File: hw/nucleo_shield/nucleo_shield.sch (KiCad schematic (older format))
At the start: 11 parts, among them CN101 Nucleo-F411RE-CN10, CN71 Nucleo-F411RE-CN7, P4 POWER_CON, P6 ETH_CONN, P7 SD_CONN, P8 LCD_CONN, P9 CONN_SCT

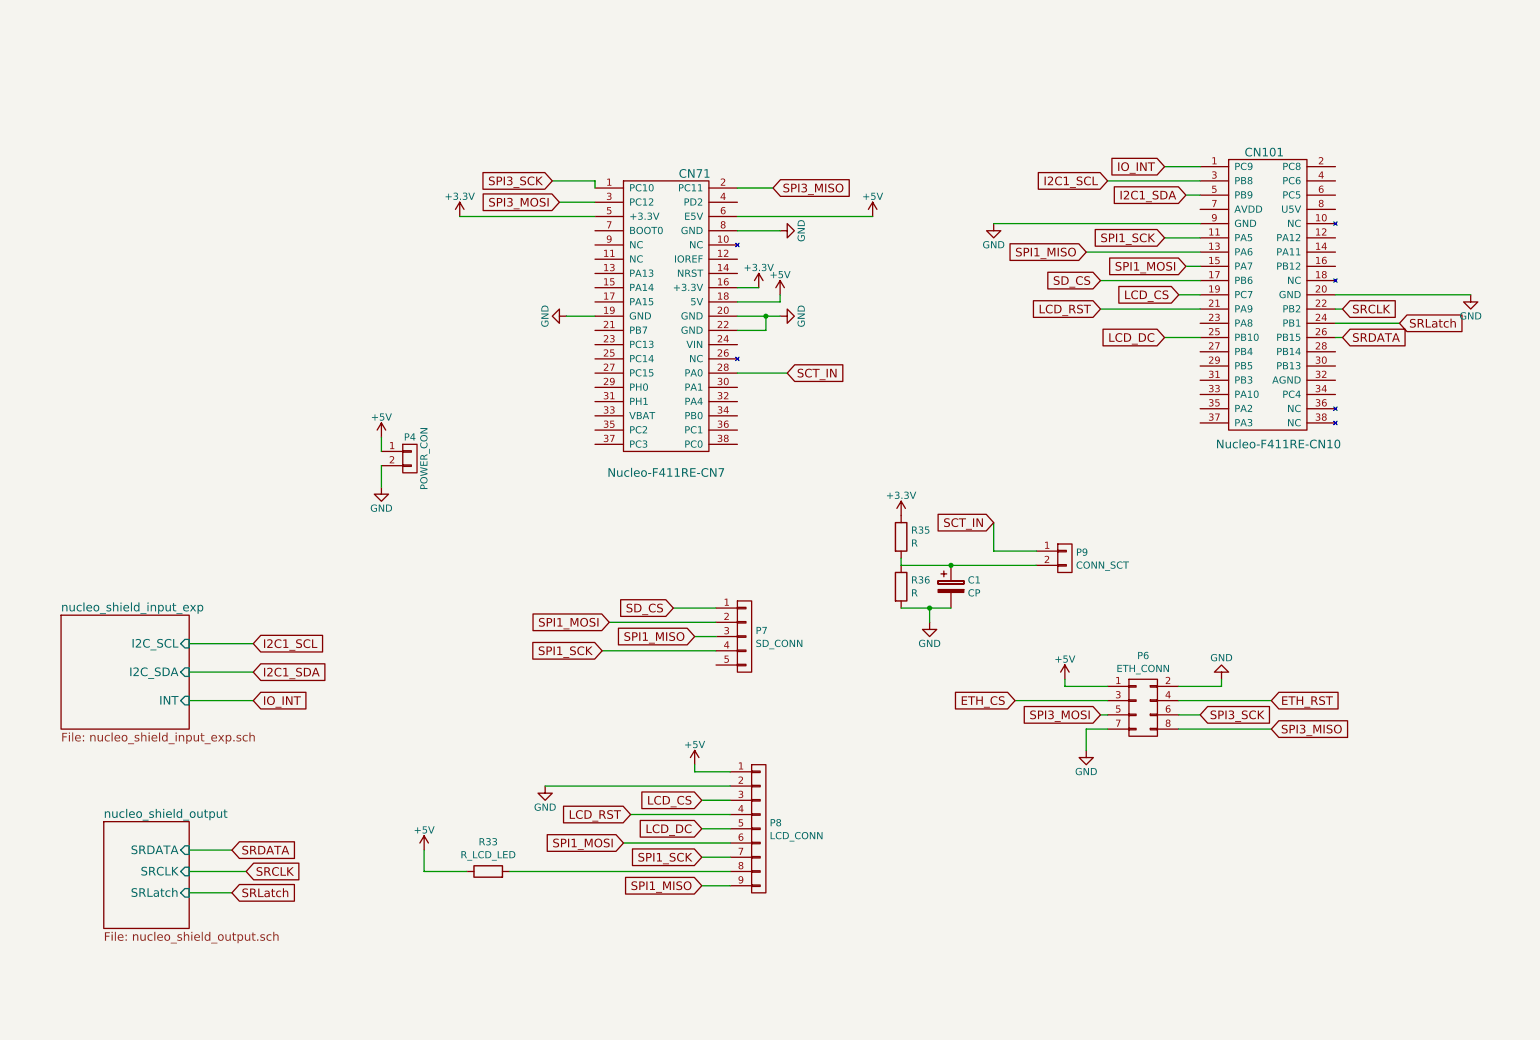
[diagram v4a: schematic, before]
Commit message: Nucleo: add RS485 headers, add CMS pulldown  resistors
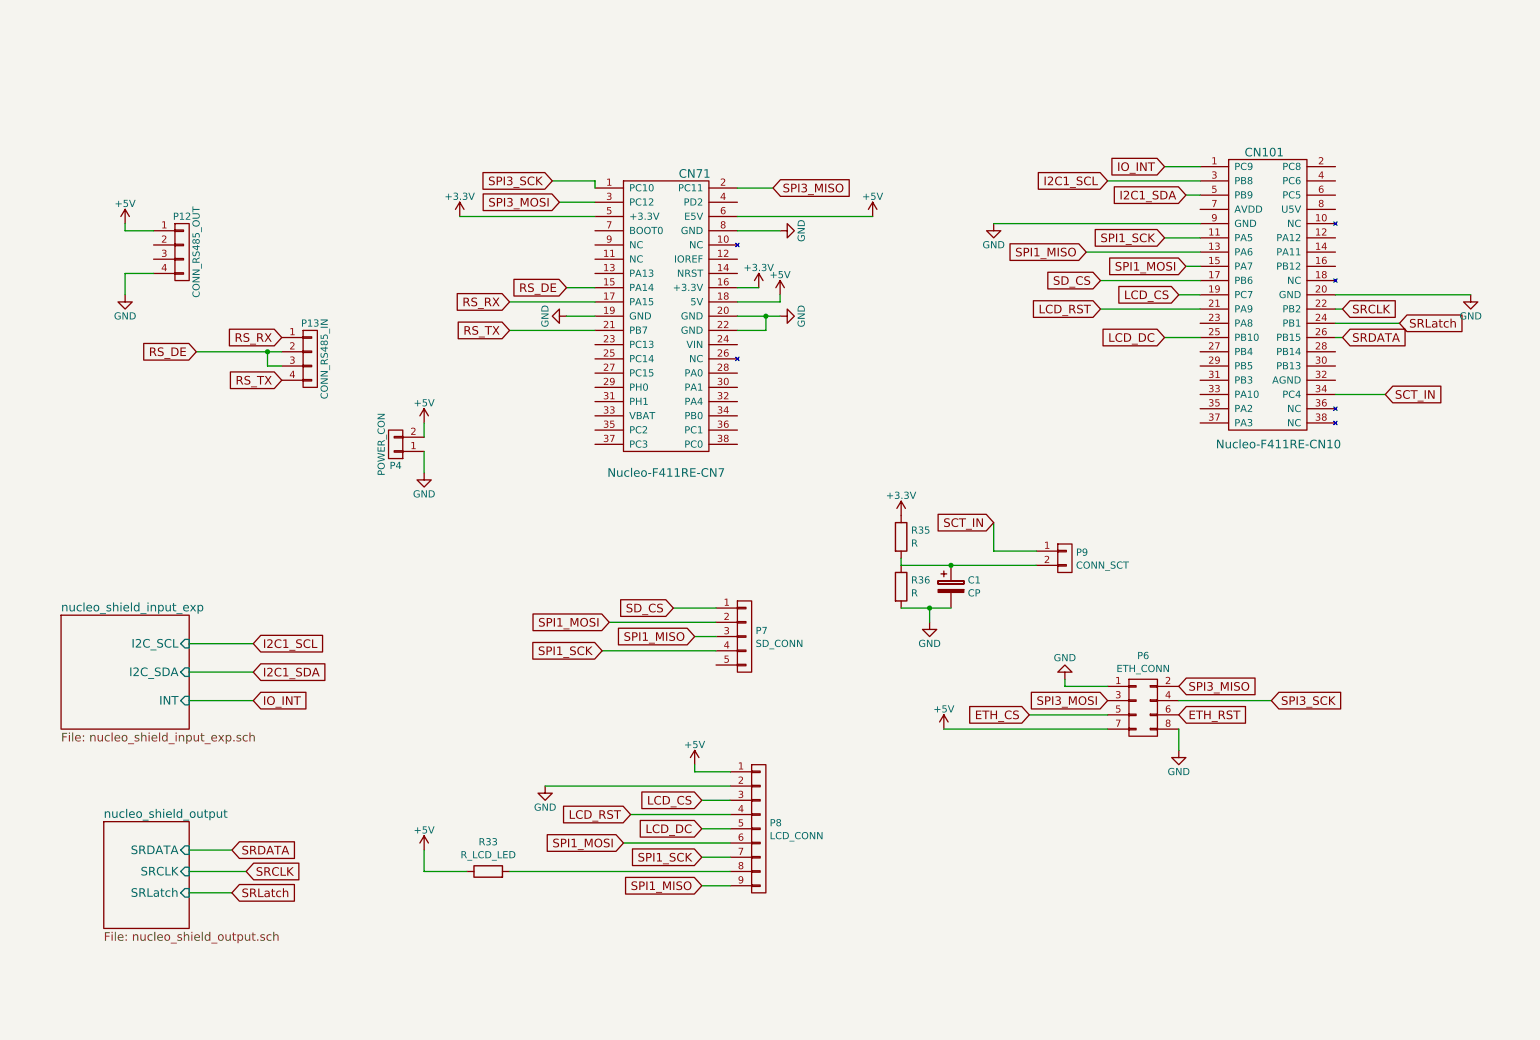
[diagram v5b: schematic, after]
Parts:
- added P12: CONN_RS485_OUT, Pin_Headers:Pin_Header_Straight_1x04, symbol CONN_01X04
- added P13: CONN_RS485_IN, Pin_Headers:Pin_Header_Straight_1x04, symbol CONN_01X04
- R33, R35, R36: footprint Resistors_ThroughHole:Resistor_Horizontal_RM10mm -> Resistors_SMD:R_0805_HandSoldering
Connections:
- net +5V: now also P4.2 (P2), P6.7 (P7), P12.1 (P1); no longer P4.1 (P1), P6.1 (P1)
- net ETH_CS: now also P6.5 (P5); no longer P6.3 (P3)
- net ETH_RST: now also P6.6 (P6); no longer P6.4 (P4)
- net GND: now also P4.1 (P1), P6.1 (P1), P6.8 (P8), P12.4 (P4); no longer P4.2 (P2), P6.2 (P2), P6.7 (P7)
- net SCT_IN: now also CN101.34 (PC4); no longer CN71.28 (PA0)
- net SPI3_MISO: now also P6.2 (P2); no longer P6.8 (P8)
- net SPI3_MOSI: now also P6.3 (P3); no longer P6.5 (P5)
- net SPI3_SCK: now also P6.4 (P4); no longer P6.6 (P6)
- net RS_DE: now reaches CN71.15 (PA14)
- net RS_DE: now also P13.2 (P2), P13.3 (P3)
- net RS_RX: now reaches CN71.17 (PA15)
- net RS_RX: now also P13.1 (P1)
- net RS_TX: now reaches CN71.21 (PB7)
- net RS_TX: now also P13.4 (P4)
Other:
- moved on the sheet: P4
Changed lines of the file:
@@
 LIBS:memory
 LIBS:xilinx
+LIBS:special
 LIBS:microcontrollers
 LIBS:dsp
@@
 L CONN_01X02 P4
 U 1 1 56AB61A1
-P 3400 3700
-F 0 "P4" H 3400 3850 50  0000 C CNN
-F 1 "POWER_CON" V 3500 3700 50  0000 C CNN
-F 2 "w_conn_screw:mors_2p" H 3400 3700 60  0001 C CNN
-F 3 "" H 3400 3700 60  0000 C CNN
-	1    3400 3700
-	1    0    0    -1
+P 3300 3600
+F 0 "P4" H 3300 3750 50  0000 C CNN
+F 1 "POWER_CON" V 3400 3600 50  0000 C CNN
+F 2 "w_conn_screw:mors_2p" H 3300 3600 60  0001 C CNN
+F 3 "" H 3300 3600 60  0000 C CNN
+	1    3300 3600
+	-1   0    0    1
 $EndComp
 $Comp
 L +5V #PWR09
 U 1 1 56AB6530
-P 3200 3550
-F 0 "#PWR09" H 3200 3400 50  0001 C CNN
-F 1 "+5V" H 3200 3690 50  0000 C CNN
-F 2 "" H 3200 3550 60  0000 C CNN
-F 3 "" H 3200 3550 60  0000 C CNN
-	1    3200 3550
+P 3500 3450
+F 0 "#PWR09" H 3500 3300 50  0001 C CNN
+F 1 "+5V" H 3500 3590 50  0000 C CNN
+F 2 "" H 3500 3450 60  0000 C CNN
+F 3 "" H 3500 3450 60  0000 C CNN
+	1    3500 3450
 	1    0    0    -1
 $EndComp
@@
 L GND #PWR010
 U 1 1 56AB6589
-P 3200 3900
-F 0 "#PWR010" H 3200 3650 50  0001 C CNN
-F 1 "GND" H 3200 3750 50  0000 C CNN
-F 2 "" H 3200 3900 60  0000 C CNN
-F 3 "" H 3200 3900 60  0000 C CNN
-	1    3200 3900
+P 3500 3800
+F 0 "#PWR010" H 3500 3550 50  0001 C CNN
+F 1 "GND" H 3500 3650 50  0000 C CNN
+F 2 "" H 3500 3800 60  0000 C CNN
+F 3 "" H 3500 3800 60  0000 C CNN
+	1    3500 3800
 	1    0    0    -1
 $EndComp
@@
 	9900 2850 9950 2850
 Wire Wire Line
-	3200 3650 3200 3550
-Wire Wire Line
-	3200 3750 3200 3900
+	3500 3550 3500 3450
+Wire Wire Line
+	3500 3650 3500 3800
 Wire Wire Line
 	3750 2000 4700 2000
@@
 L +5V #PWR012
 U 1 1 572A65CF
+P 7150 5600
+F 0 "#PWR012" H 7150 5450 50  0001 C CNN
+F 1 "+5V" H 7150 5740 50  0000 C CNN
+F 2 "" H 7150 5600 60  0000 C CNN
+F 3 "" H 7150 5600 60  0000 C CNN
+	1    7150 5600
+	1    0    0    -1
+$EndComp
+$Comp
+L GND #PWR013
+U 1 1 572A660A
 P 8000 5250
-F 0 "#PWR012" H 8000 5100 50  0001 C CNN
-F 1 "+5V" H 8000 5390 50  0000 C CNN
+F 0 "#PWR013" H 8000 5000 50  0001 C CNN
+F 1 "GND" H 8000 5100 50  0000 C CNN
 F 2 "" H 8000 5250 60  0000 C CNN
 F 3 "" H 8000 5250 60  0000 C CNN
 	1    8000 5250
-	1    0    0    -1
-$EndComp
-$Comp
-L GND #PWR013
-U 1 1 572A660A
-P 9100 5250
-F 0 "#PWR013" H 9100 5000 50  0001 C CNN
-F 1 "GND" H 9100 5100 50  0000 C CNN
-F 2 "" H 9100 5250 60  0000 C CNN
-F 3 "" H 9100 5250 60  0000 C CNN
-	1    9100 5250
-	-1   0    0    1
-$EndComp
-Wire Wire Line
-	8800 5300 9100 5300
-Wire Wire Line
-	9100 5300 9100 5250
-Wire Wire Line
-	8000 5250 8000 5300
-Wire Wire Line
-	8000 5300 8300 5300
-Text GLabel 9450 5400 2    60   Input ~ 0
+	1    0    0    1
+$EndComp
+Wire Wire Line
+	8300 5300 8000 5300
+Wire Wire Line
+	8000 5300 8000 5250
+Text GLabel 8800 5500 2    60   Input ~ 0
 ETH_RST
-Text GLabel 7650 5400 0    60   Input ~ 0
+Text GLabel 7750 5500 0    60   Input ~ 0
 ETH_CS
 $Comp
 L GND #PWR014
 U 1 1 572A6AC8
-P 8150 5750
-F 0 "#PWR014" H 8150 5500 50  0001 C CNN
-F 1 "GND" H 8150 5600 50  0000 C CNN
-F 2 "" H 8150 5750 60  0000 C CNN
-F 3 "" H 8150 5750 60  0000 C CNN
-	1    8150 5750
-	1    0    0    -1
-$EndComp
-Wire Wire Line
-	7650 5400 8300 5400
-Wire Wire Line
-	8250 5500 8300 5500
-Wire Wire Line
-	8300 5600 8150 5600
-Wire Wire Line
-	8150 5600 8150 5750
+P 8800 5750
+F 0 "#PWR014" H 8800 5500 50  0001 C CNN
+F 1 "GND" H 8800 5600 50  0000 C CNN
+F 2 "" H 8800 5750 60  0000 C CNN
+F 3 "" H 8800 5750 60  0000 C CNN
+	1    8800 5750
+	1    0    0    -1
+$EndComp
+Wire Wire Line
+	7750 5500 8300 5500
+Wire Wire Line
+	8800 5600 8800 5750
 Wire Wire Line
 	8800 5400 9450 5400
-Wire Wire Line
-	8950 5500 8800 5500
-Wire Wire Line
-	8800 5600 9450 5600
-Text GLabel 8950 5500 2    60   Input ~ 0
+Text GLabel 9450 5400 2    60   Input ~ 0
 SPI3_SCK
-Text GLabel 8250 5500 0    60   Input ~ 0
+Text GLabel 8300 5400 0    60   Input ~ 0
 SPI3_MOSI
-Text GLabel 9450 5600 2    60   Input ~ 0
+Text GLabel 8800 5300 2    60   Input ~ 0
 SPI3_MISO
 Text GLabel 8700 2150 0    60   Input ~ 0
@@
 F 0 "R33" V 4157 6600 50  0000 C CNN
 F 1 "R_LCD_LED" V 4066 6600 50  0000 C CNN
-F 2 "Resistors_ThroughHole:Resistor_Horizontal_RM10mm" V 3880 6600 50  0001 C CNN
+F 2 "Resistors_SMD:R_0805_HandSoldering" V 3880 6600 50  0001 C CNN
 F 3 "" H 3950 6600 50  0000 C CNN
 	1    3950 6600
@@
 	1    0    0    -1
 $EndComp
-Text GLabel 6050 3100 2    60   Input ~ 0
+Text GLabel 10250 3250 2    60   Input ~ 0
 SCT_IN
 Wire Wire Line
-	5700 3100 6050 3100
+	9900 3250 10250 3250
 Text GLabel 7500 4150 0    60   Input ~ 0
 SCT_IN
@@
 F 0 "R35" H 6920 4296 50  0000 L CNN
 F 1 "R" H 6920 4205 50  0000 L CNN
-F 2 "Resistors_ThroughHole:Resistor_Horizontal_RM10mm" V 6780 4250 50  0001 C CNN
+F 2 "Resistors_SMD:R_0805_HandSoldering" V 6780 4250 50  0001 C CNN
 F 3 "" H 6850 4250 50  0000 C CNN
 	1    6850 4250
@@
 F 0 "R36" H 6920 4646 50  0000 L CNN
 F 1 "R" H 6920 4555 50  0000 L CNN
-F 2 "Resistors_ThroughHole:Resistor_Horizontal_RM10mm" V 6780 4600 50  0001 C CNN
+F 2 "Resistors_SMD:R_0805_HandSoldering" V 6780 4600 50  0001 C CNN
 F 3 "" H 6850 4600 50  0000 C CNN
 	1    6850 4600
@@
 Wire Wire Line
 	8950 2850 8700 2850
+Text GLabel 4100 2600 0    60   Input ~ 0
+RS_RX
+Text GLabel 4100 2800 0    60   Input ~ 0
+RS_TX
+Wire Wire Line
+	4100 2600 4700 2600
+Wire Wire Line
+	4100 2800 4700 2800
+$Comp
+L CONN_01X04 P13
+U 1 1 5731D7CF
+P 2700 3000
+F 0 "P13" H 2700 3250 50  0000 C CNN
+F 1 "CONN_RS485_IN" V 2800 3000 50  0000 C CNN
+F 2 "Pin_Headers:Pin_Header_Straight_1x04" H 2700 3000 60  0001 C CNN
+F 3 "" H 2700 3000 60  0000 C CNN
+	1    2700 3000
+	1    0    0    -1
+$EndComp
+$Comp
+L CONN_01X04 P12
+U 1 1 5731D900
+P 1800 2250
+F 0 "P12" H 1800 2500 50  0000 C CNN
+F 1 "CONN_RS485_OUT" V 1900 2250 50  0000 C CNN
+F 2 "Pin_Headers:Pin_Header_Straight_1x04" H 1800 2250 60  0001 C CNN
+F 3 "" H 1800 2250 60  0000 C CNN
+	1    1800 2250
+	1    0    0    -1
+$EndComp
+Text GLabel 4500 2500 0    60   Input ~ 0
+RS_DE
+Wire Wire Line
+	4700 2500 4500 2500
+Text GLabel 1900 2950 0    60   Input ~ 0
+RS_DE
+Wire Wire Line
+	1900 2950 2500 2950
+Wire Wire Line
+	2400 2950 2400 3050
+Wire Wire Line
+	2400 3050 2500 3050
+Connection ~ 2400 2950
+Text GLabel 2500 3150 0    60   Input ~ 0
+RS_TX
+Text GLabel 2500 2850 0    60   Input ~ 0
+RS_RX
+$Comp
+L +5V #PWR020
+U 1 1 5731E393
+P 1400 2050
+F 0 "#PWR020" H 1400 1900 50  0001 C CNN
+F 1 "+5V" H 1400 2190 50  0000 C CNN
+F 2 "" H 1400 2050 60  0000 C CNN
+F 3 "" H 1400 2050 60  0000 C CNN
+	1    1400 2050
+	1    0    0    -1
+$EndComp
+$Comp
+L GND #PWR021
+U 1 1 5731E3CA
+P 1400 2550
+F 0 "#PWR021" H 1400 2300 50  0001 C CNN
+F 1 "GND" H 1400 2400 50  0000 C CNN
+F 2 "" H 1400 2550 60  0000 C CNN
+F 3 "" H 1400 2550 60  0000 C CNN
+	1    1400 2550
+	1    0    0    -1
+$EndComp
+Wire Wire Line
+	1400 2050 1400 2100
+Wire Wire Line
+	1400 2100 1600 2100
+Wire Wire Line
+	1600 2400 1400 2400
+Wire Wire Line
+	1400 2400 1400 2550
+Wire Wire Line
+	8300 5600 7150 5600
 $EndSCHEMATC

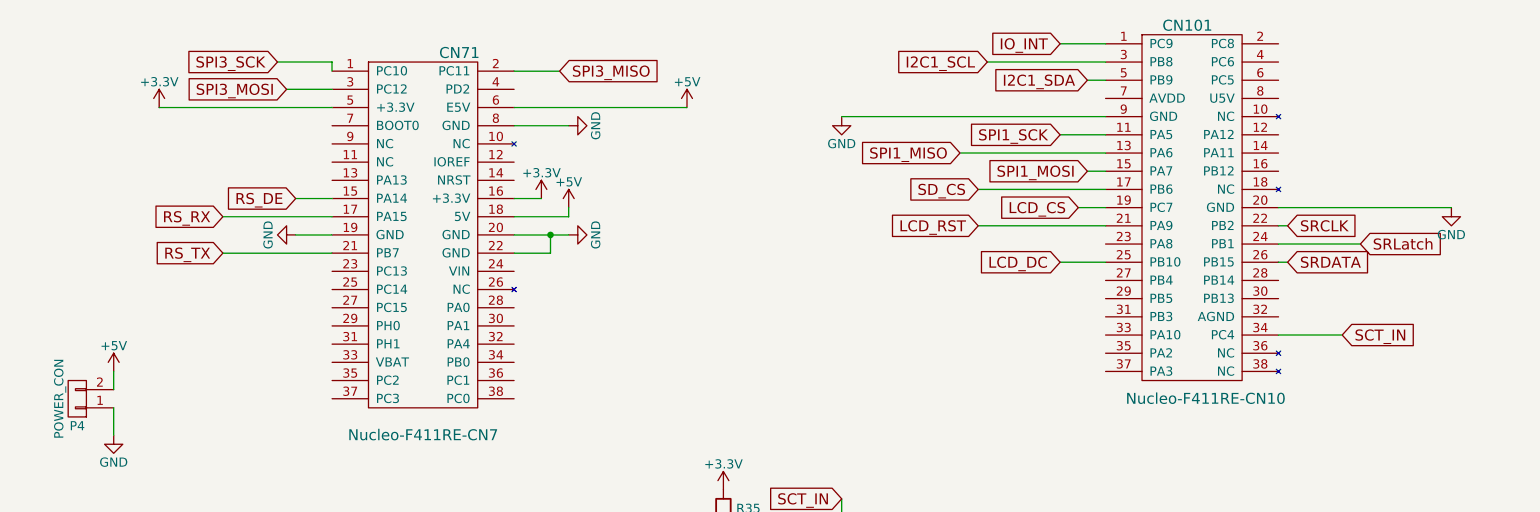
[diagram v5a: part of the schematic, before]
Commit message: Nucleo: Rework connection
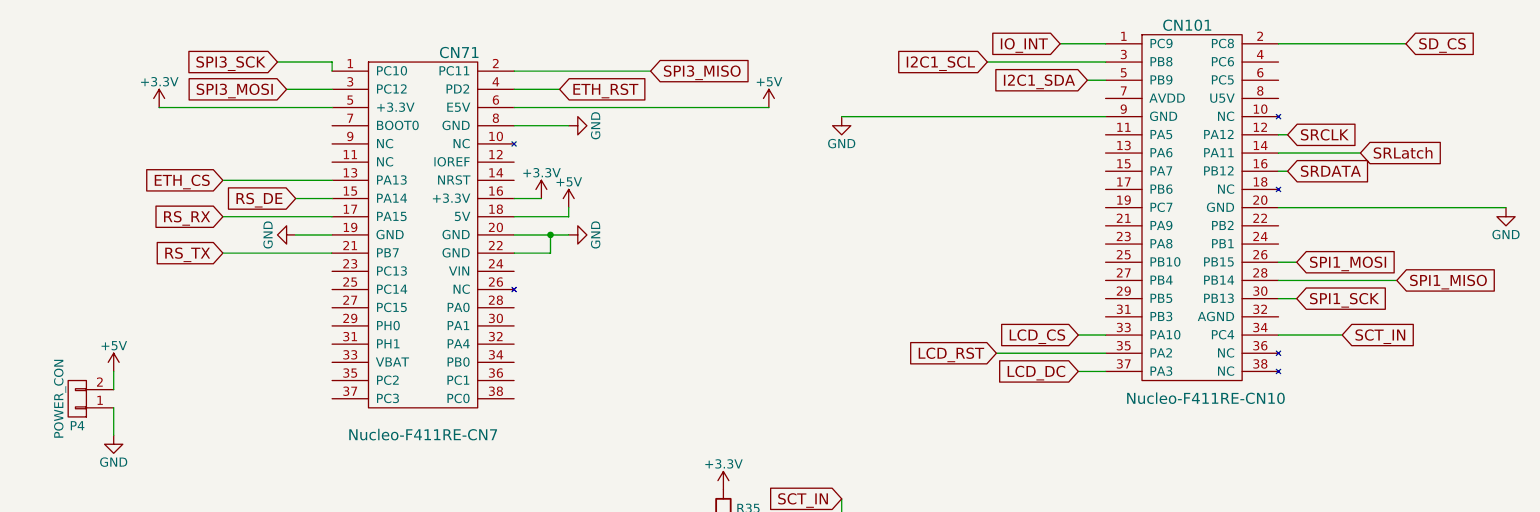
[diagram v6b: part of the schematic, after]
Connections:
- net ETH_CS: now also CN71.13 (PA13)
- net ETH_RST: now also CN71.4 (PD2)
- net LCD_CS: now also CN101.33 (PA10); no longer CN101.19 (PC7)
- net LCD_DC: now also CN101.37 (PA3); no longer CN101.25 (PB10)
- net LCD_RST: now also CN101.35 (PA2); no longer CN101.21 (PA9)
- net SD_CS: now also CN101.2 (PC8); no longer CN101.17 (PB6)
- net SPI1_MISO: now also CN101.28 (PB14); no longer CN101.13 (PA6)
- net SPI1_MOSI: now also CN101.26 (PB15); no longer CN101.15 (PA7)
- net SPI1_SCK: now also CN101.30 (PB13); no longer CN101.11 (PA5)
- net SRCLK: now also CN101.12 (PA12); no longer CN101.22 (PB2)
- net SRDATA: now also CN101.16 (PB12); no longer CN101.26 (PB15)
- net SRLatch: now also CN101.14 (PA11); no longer CN101.24 (PB1)
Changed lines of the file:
@@
 LIBS:memory
 LIBS:xilinx
-LIBS:special
 LIBS:microcontrollers
 LIBS:dsp
@@
 	1    0    0    -1
 $EndComp
-Text GLabel 10350 2750 2    60   Input ~ 0
+Text GLabel 10350 2250 2    60   Input ~ 0
 SRLatch
-Text GLabel 9950 2650 2    60   Input ~ 0
+Text GLabel 9950 2150 2    60   Input ~ 0
 SRCLK
 $Comp
 L GND #PWR01
 U 1 1 56699180
-P 10850 2550
-F 0 "#PWR01" H 10850 2300 50  0001 C CNN
-F 1 "GND" H 10850 2400 50  0000 C CNN
-F 2 "" H 10850 2550 60  0000 C CNN
-F 3 "" H 10850 2550 60  0000 C CNN
-	1    10850 2550
-	1    0    0    -1
-$EndComp
-Text GLabel 9950 2850 2    60   Input ~ 0
+P 11150 2550
+F 0 "#PWR01" H 11150 2300 50  0001 C CNN
+F 1 "GND" H 11150 2400 50  0000 C CNN
+F 2 "" H 11150 2550 60  0000 C CNN
+F 3 "" H 11150 2550 60  0000 C CNN
+	1    11150 2550
+	1    0    0    -1
+$EndComp
+Text GLabel 9950 2350 2    60   Input ~ 0
 SRDATA
 $Comp
@@
 L +5V #PWR08
 U 1 1 56AB5C14
-P 6650 2000
-F 0 "#PWR08" H 6650 1850 50  0001 C CNN
-F 1 "+5V" H 6650 2140 50  0000 C CNN
-F 2 "" H 6650 2000 60  0000 C CNN
-F 3 "" H 6650 2000 60  0000 C CNN
-	1    6650 2000
+P 7100 2000
+F 0 "#PWR08" H 7100 1850 50  0001 C CNN
+F 1 "+5V" H 7100 2140 50  0000 C CNN
+F 2 "" H 7100 2000 60  0000 C CNN
+F 3 "" H 7100 2000 60  0000 C CNN
+	1    7100 2000
 	1    0    0    -1
 $EndComp
@@
 SRDATA
 Wire Wire Line
-	9950 2650 9900 2650
-Wire Wire Line
-	9900 2550 10850 2550
+	9950 2150 9900 2150
+Wire Wire Line
+	9900 2550 11150 2550
 Wire Wire Line
 	4500 2700 4700 2700
@@
 Connection ~ 5900 2700
 Wire Wire Line
-	10350 2750 9900 2750
-Wire Wire Line
-	9900 2850 9950 2850
+	10350 2250 9900 2250
+Wire Wire Line
+	9900 2350 9950 2350
 Wire Wire Line
 	3500 3550 3500 3450
@@
 	3750 2000 4700 2000
 Wire Wire Line
-	6650 2000 5700 2000
+	7100 2000 5700 2000
 Wire Wire Line
 	1850 6450 2150 6450
@@
 Wire Wire Line
 	8300 1750 8950 1750
-Text GLabel 5950 1800 2    60   Input ~ 0
+Text GLabel 6450 1800 2    60   Input ~ 0
 SPI3_MISO
 Text GLabel 4450 1900 0    60   Input ~ 0
@@
 SPI3_SCK
 Wire Wire Line
-	5950 1800 5700 1800
+	6450 1800 5700 1800
 Wire Wire Line
 	4400 1750 4700 1750
@@
 Text GLabel 8800 5300 2    60   Input ~ 0
 SPI3_MISO
-Text GLabel 8700 2150 0    60   Input ~ 0
+Text GLabel 10000 3050 2    60   Input ~ 0
 SPI1_SCK
-Text GLabel 8150 2250 0    60   Input ~ 0
+Text GLabel 10550 2950 2    60   Input ~ 0
 SPI1_MISO
-Text GLabel 8850 2350 0    60   Input ~ 0
+Text GLabel 10000 2850 2    60   Input ~ 0
 SPI1_MOSI
-Text GLabel 8250 2450 0    60   Input ~ 0
-SD_CS
 $Comp
 L CONN_01X05 P7
@@
 Wire Wire Line
 	5650 6000 4350 6000
-Text GLabel 8800 2550 0    60   Input ~ 0
+Text GLabel 8800 3250 0    60   Input ~ 0
 LCD_CS
 Wire Wire Line
-	8700 2150 8950 2150
-Wire Wire Line
-	8950 2250 8150 2250
-Wire Wire Line
-	8850 2350 8950 2350
-Wire Wire Line
-	8250 2450 8950 2450
-Wire Wire Line
-	8950 2550 8800 2550
+	10000 3050 9900 3050
+Wire Wire Line
+	9900 2950 10550 2950
+Wire Wire Line
+	10000 2850 9900 2850
+Wire Wire Line
+	8950 3250 8800 3250
 Text GLabel 5450 6100 0    60   Input ~ 0
 LCD_CS
@@
 Text GLabel 5450 6300 0    60   Input ~ 0
 LCD_DC
-Text GLabel 8250 2650 0    60   Input ~ 0
+Text GLabel 8350 3350 0    60   Input ~ 0
 LCD_RST
-Text GLabel 8700 2850 0    60   Input ~ 0
+Text GLabel 8800 3450 0    60   Input ~ 0
 LCD_DC
 Wire Wire Line
-	8950 2650 8250 2650
+	8950 3350 8350 3350
 Wire Wire Line
 	5650 6200 4950 6200
@@
 	7500 4350 7800 4350
 Wire Wire Line
-	8950 2850 8700 2850
+	8950 3450 8800 3450
 Text GLabel 4100 2600 0    60   Input ~ 0
 RS_RX
@@
 Wire Wire Line
 	8300 5600 7150 5600
+Text GLabel 5950 1900 2    60   Input ~ 0
+ETH_RST
+Wire Wire Line
+	5700 1900 5950 1900
+Text GLabel 4100 2400 0    60   Input ~ 0
+ETH_CS
+Wire Wire Line
+	4100 2400 4700 2400
+Text GLabel 10600 1650 2    60   Input ~ 0
+SD_CS
+Wire Wire Line
+	10600 1650 9900 1650
 $EndSCHEMATC
